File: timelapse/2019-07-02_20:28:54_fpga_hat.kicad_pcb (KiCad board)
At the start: 4 copper layers, 65 x 56.5 mm, 90 parts, among them J1 2x20, J2 AudioJack3, J3 Conn_02x06_Top_Bottom, J4 Conn_02x06_Top_Bottom, J5 Conn_02x06_Top_Bottom, J6 Conn_01x02, SW1 PTS815, SW2 PTS815, SW3 PTS815, SW4 PTS815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

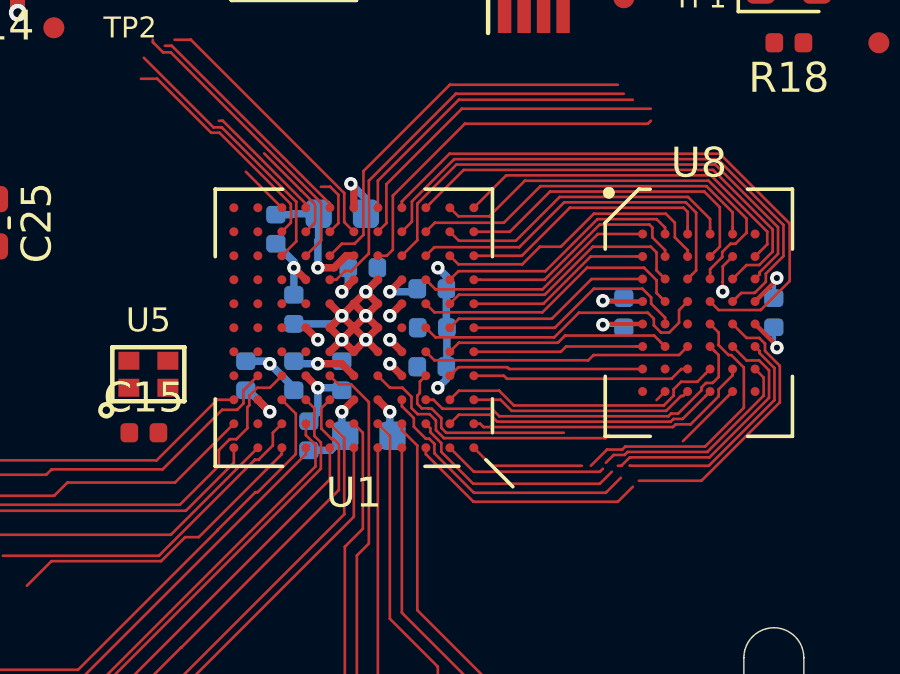
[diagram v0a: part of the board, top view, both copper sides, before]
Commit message: SRAM escaped. Some work on FPGA power routing. Some SRAM pinswapping.
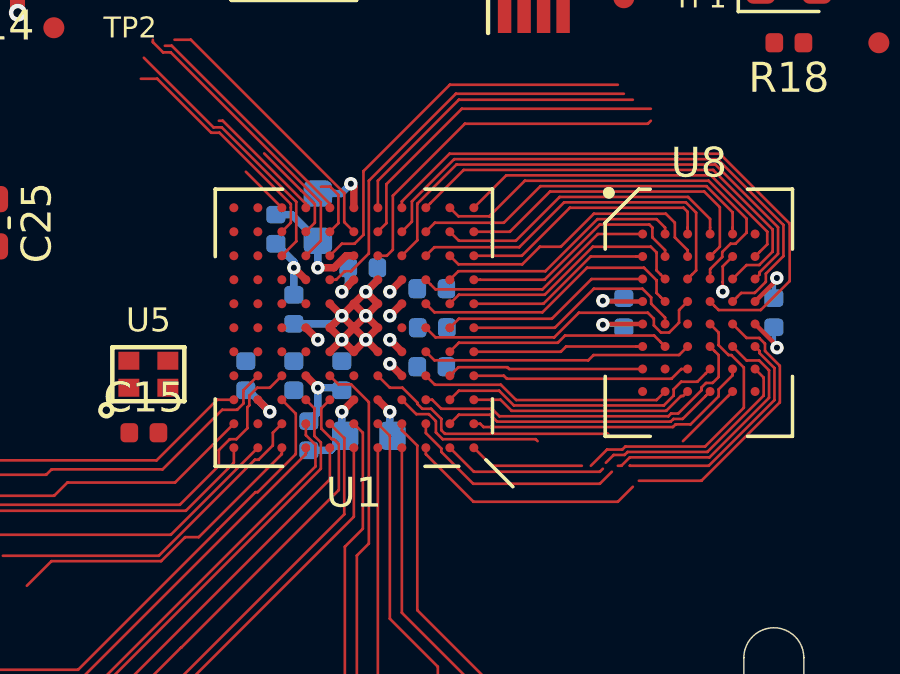
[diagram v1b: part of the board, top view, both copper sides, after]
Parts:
- moved C2 0.82 mm to (131.3, 102.8), turned to 90 degrees
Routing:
- net GND: track 24.9 -> 18.6 mm, vias 11 -> 8
- net /SRAM_A11: track 11.6 -> 7.66 mm
- net +3V3: track 10.9 -> 8.68 mm, vias 8 -> 7
- net /SRAM_A8: track 6.93 -> 8.43 mm
- net +1V2: track 12.7 -> 11.7 mm
- net Net-(C2-Pad1): track 4.61 -> 4.03 mm
